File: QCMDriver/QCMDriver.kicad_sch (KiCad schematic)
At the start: 26 parts, among them J1 Conn_Coaxial, J2 Conn_Coaxial, J3 Conn_Coaxial, Q1 BC817, U1 74LVC1GU04DRL, U2 74LVC1GU04DRL

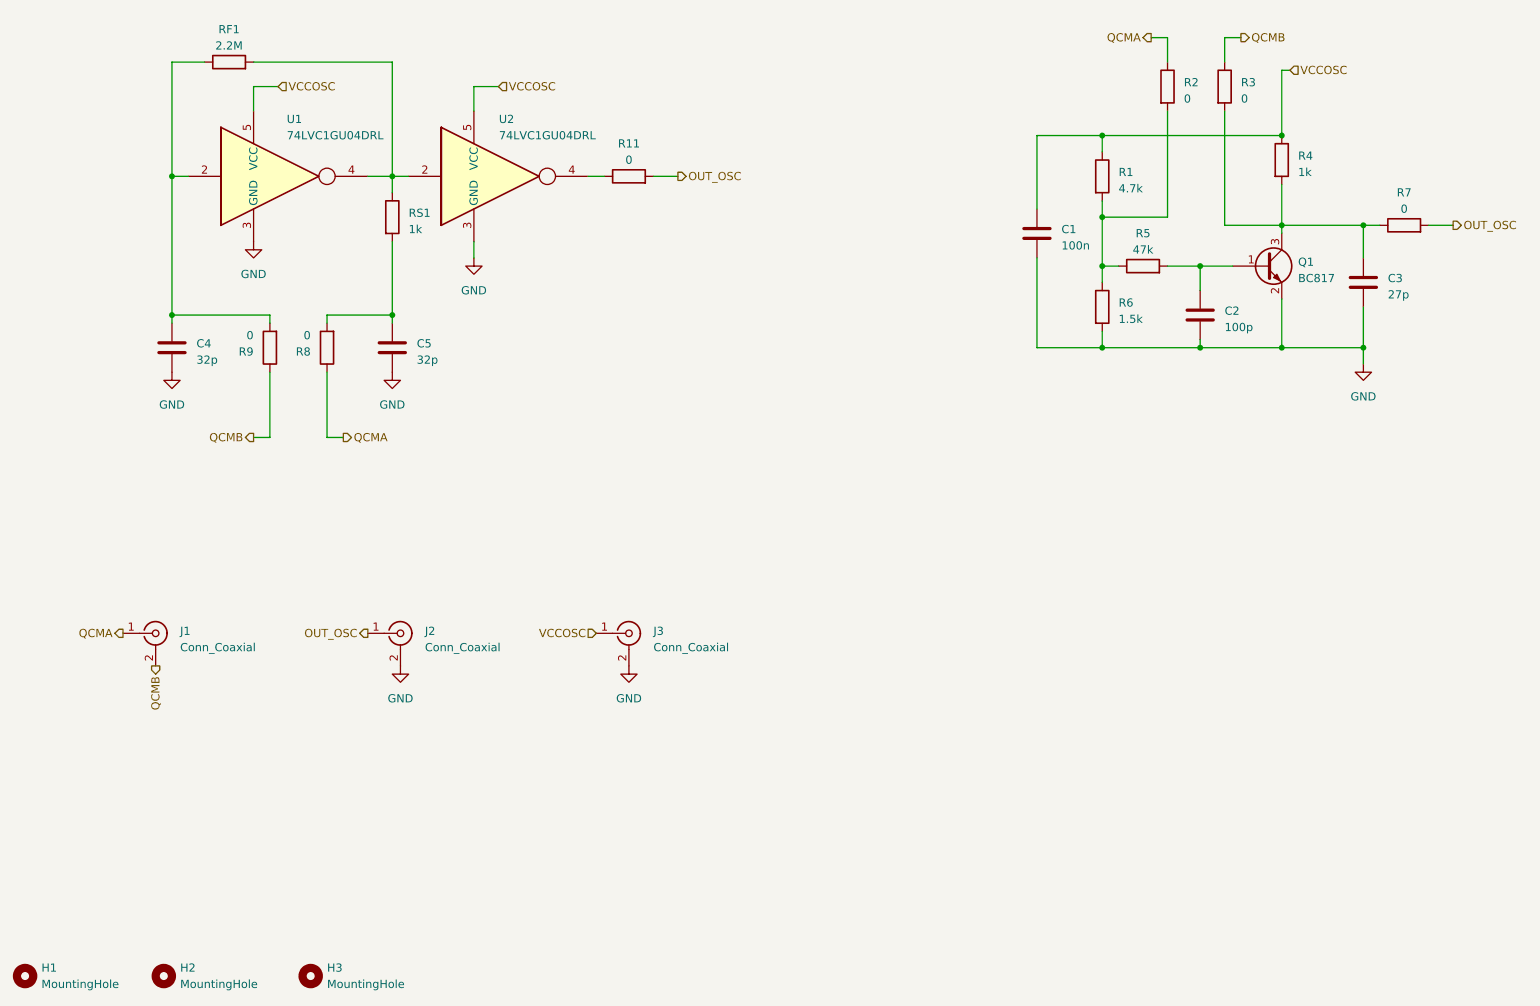
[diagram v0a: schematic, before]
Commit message: vcc caps and vias added, minor layout improvements
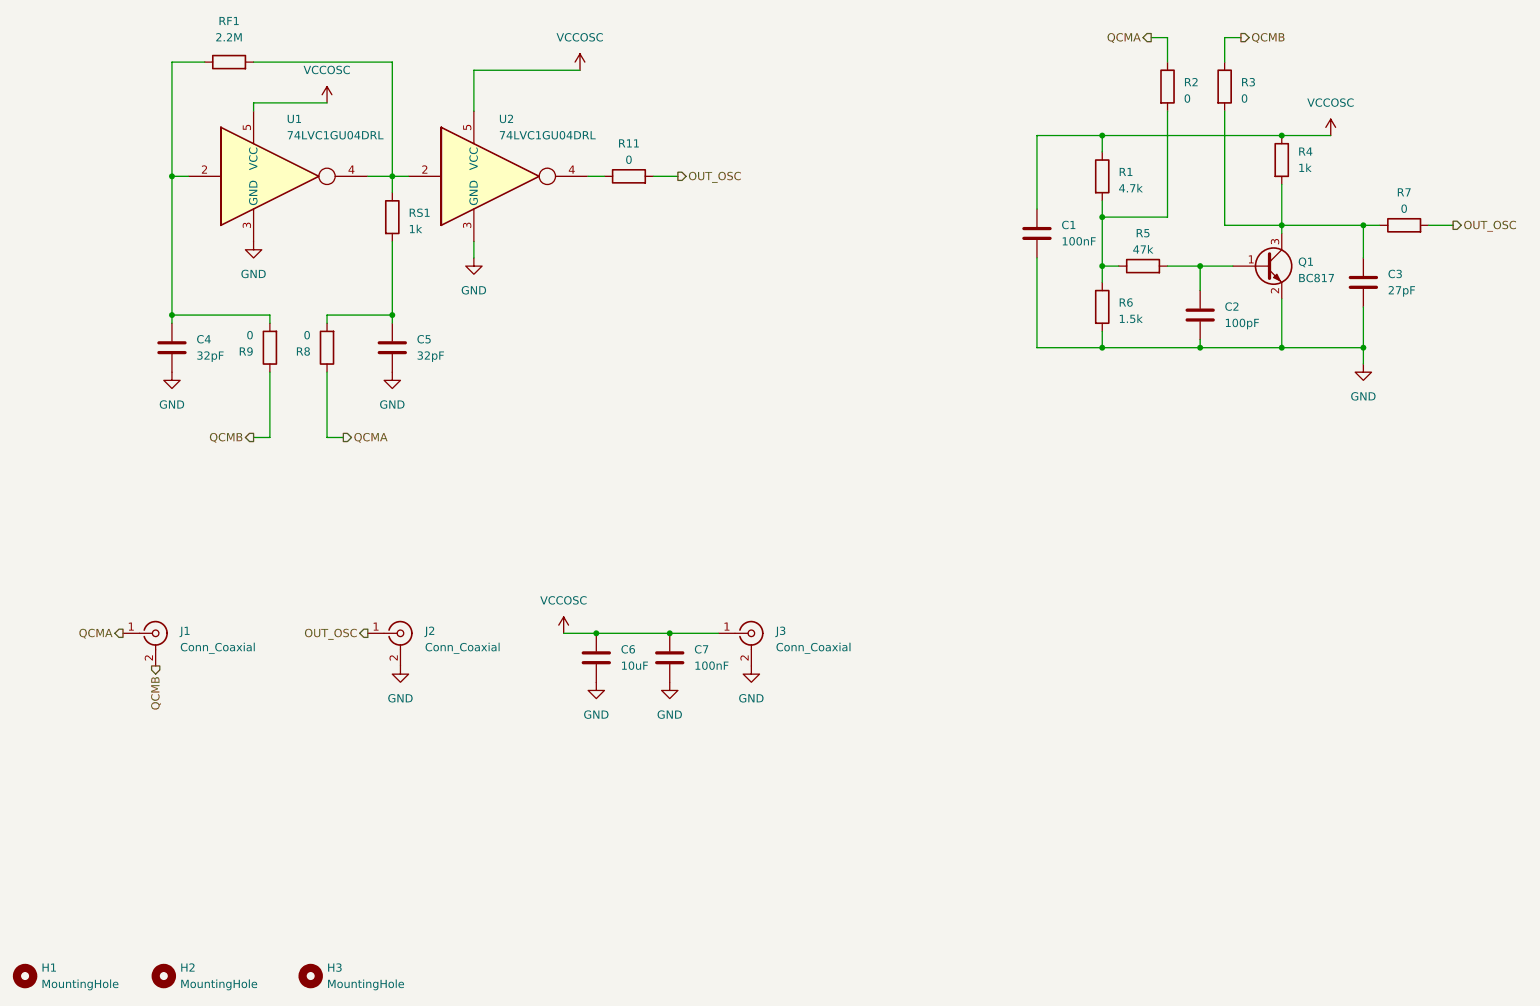
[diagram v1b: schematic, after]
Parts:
- added C6: 10uF, Capacitor_SMD:C_0603_1608Metric, symbol Device:C
- added C7: 100nF, Capacitor_SMD:C_0603_1608Metric, symbol Device:C
- C1: value 100n -> 100nF
- C2: value 100p -> 100pF
- C3: value 27p -> 27pF
- C4, C5: value 32p -> 32pF
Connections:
- net GND: now also C6.2, C7.2
- net VCCOSC: now also C6.1, C7.1
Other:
- moved on the sheet: J3
